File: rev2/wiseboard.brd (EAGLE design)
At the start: 87 x 67 mm, 85 parts, among them IC2 LM358MX, Q1 IRLML6402TRPBF, Q2 IRLML6402TRPBF, U1 LT1945EMSPBF, U2 BQ24210DQCT, X1 1528-1438-ND

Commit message: begin rev2 overall
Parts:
- removed C11, C12: 100nF, adafruit:C1206
- removed ESPDEBUG_1, ESPDEBUG_2: (no value), pinhead:1X08
- removed INPUTBUTTONHEADER: (no value), pinhead:1X02
- removed JP3: JUMPER, Sparkfun-Passives:SMT-JUMPER_2_NC_PASTE_NO-SILK
- removed R20, R24, R25: 10K, adafruit:R1206
- removed U$11, U$12: 1727-3473-ND, WISE:SO16
- removed U$13: FSA3157, WISE:SC70-6L
- removed X1: 1528-1438-ND, adafruit:ESP-12
- added R11, R12: 10k, resistor:R0805
- added U3: ESP-WROOM-03, esp32:ESP-WROOM-03
- C1, C16, C2, C3, C4, C5, C6, C7, C8, C9: device adafruit:C1206 -> resistor:C0805
- R1, R10, R13, R14, R2, R28, R29, R3, R30, R31, R32, R33, R34, R35, R4, R9: device adafruit:M1206 -> resistor:R0805
- R21, R22, R23, R36, R37, R38, R5, R6, R7, R8: device adafruit:R1206 -> resistor:R0805
- U$4: value HFQ339CT-ND -> FH26W-39S
- moved POWERGOOD 164.2 mm to (-74.9, 3.81), turned to 0 degrees
- moved R10 156.7 mm to (-81.3, 64.8)
- moved U2 151.2 mm to (-76.2, 82.5)
- moved R38 141.7 mm to (-74.9, 64.8), turned to 0 degrees
- moved U$14 140.6 mm to (-83.8, 77.5), turned to 0 degrees
- moved S6 140.3 mm to (-76.2, 38.1), turned to 0 degrees
- moved S5 139.5 mm to (-64.8, 38.1)
- moved D2 139.2 mm to (-82.5, 82.5), turned to 0 degrees
- moved D1 139.2 mm to (-57.1, 82.5)
- moved JP4 138.0 mm to (-50.8, 82.5), flipped to the top, turned to 0 degrees
- moved R31 136.1 mm to (-80.0, 71.1), turned to 0 degrees
- moved S4 135.5 mm to (-53.3, 38.1), turned to 0 degrees
- moved C7 134.2 mm to (-82.5, 55.9), turned to 0 degrees
- moved C9 133.4 mm to (-62.2, 64.8)
- moved CHRG/LBO 131.7 mm to (-45.7, 24.1), turned to 0 degrees
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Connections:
- removed net ADC: ESPDEBUG_1.2, R28.1, R29.2, X1.2
- removed net CH_PD: ESPDEBUG_1.3, R20.1, X1.3
- removed net GPIO12: ESPDEBUG_1.6, U$12.1, U$23.2, X1.6
- removed net GPIO13: ESPDEBUG_1.7, U$11.2, U$12.2, U$23.5, X1.7
- removed net GPIO14: ESPDEBUG_1.5, U$11.3, U$12.3, U$23.6, X1.5
- removed net GPIO15: ESPDEBUG_2.7, R25.2, U$23.1, X1.10
- removed net GPIO16: ESPDEBUG_1.4, JP3.2, X1.4
- removed net QP0: U$11.4, U$4.P$12
- removed net QP1: U$11.5, U$4.P$13
- removed net QP2: U$11.6, U$4.P$14
- removed net QP2@2: U$12.6, U$4.P$32, U$4.P$37
- removed net QP3: U$11.7, U$4.P$15
- removed net QP4: U$11.14, U$4.P$16
- removed net QP5: U$11.13, U$4.P$17
- removed net QP6: U$11.12, U$4.P$18
- removed net QP6@2: U$12.12, U$4.P$27, U$4.P$28
- removed net QP7: U$11.11, U$4.P$19
- removed net QP7@2: U$12.11, U$4.P$33, U$4.P$38
- new net 15V: U$4.P$2
- new net CKV: U$4.P$33, U$4.P$38, U3.37
- new net D0: U$4.P$12, U3.26
- new net D1: U$4.P$13, U3.27
- new net D2: U$4.P$14, U3.13
- new net D3: U$4.P$15, U3.28
- new net D4: U$4.P$16, U3.12
- new net D5: U$4.P$17, U3.29
- new net D6: U$4.P$18, U3.30
- new net D7: U$4.P$19, U3.31
- new net GMODE: U$4.P$27, U$4.P$28
- new net N$24: U3.35
- new net N$25: U3.34
- new net N$32: U3.25
- new net N$37: U3.14
- new net N$41: U3.33
- new net N$44: U3.11
- new net N$46: U3.8
- new net N$48: U3.6
- new net N$49: U3.7
- new net N$50: U3.4
- new net N$51: U3.5
- new net SPV: U$4.P$32, U$4.P$37, U3.36
- net +15V: no longer U$4.P$2
- net +3V3: now also U$4.P$10, U$4.P$29, U$4.P$30, U$4.P$35, U$4.P$36, U$4.P$4, U$4.P$8; no longer ESPDEBUG_1.8, INPUTBUTTONHEADER.1, R20.2, R24.2, U$13.5, X1.8
- net BOOSTENA: no longer ESPDEBUG_2.6, Q2.1, R24.1, X1.11
- net CL: now also U3.23; no longer ESPDEBUG_2.4, X1.13
- net GND: now also R11.1, R12.1, U3.1, U3.15, U3.38, U3.GND; no longer C11.2, C12.2, ESPDEBUG_2.8, R25.1, R29.1, U$11.8, U$12.8, U$13.2, X1.9
- net GPIO0: no longer ESPDEBUG_2.5, X1.12
- net LE: now also U3.16; no longer U$12.14
- net N$12: no longer U$13.4
- net N$26: no longer INPUTBUTTONHEADER.2, U$13.1
- net NEGEN: now also R11.2, U3.9; no longer U$12.5
- net OE: now also U3.24; no longer ESPDEBUG_2.3, X1.14
- net POSEN: now also R12.2, U3.10; no longer U$12.4
- net RESET: no longer ESPDEBUG_1.1, JP3.1, X1.1
- net RXD: no longer ESPDEBUG_2.2, U$13.6, X1.15
- net SPH: no longer U$12.13
- net TXD: no longer ESPDEBUG_2.1, X1.16
- net VBAT: no longer U$13.3
- net VDD: no longer C11.1, C12.1, U$11.1, U$11.15, U$11.16, U$12.15, U$12.16, U$4.P$10, U$4.P$29, U$4.P$30, U$4.P$35, U$4.P$36, U$4.P$4, U$4.P$8
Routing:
- net +3V3: track 287.7 -> 0.00 mm, vias 9 -> 0
- net GND: track 141.5 -> 0.00 mm, vias 38 -> 0
- net VDD: track 139.3 -> 0.00 mm, vias 8 -> 0
- net VBAT: track 125.0 -> 0.00 mm, vias 3 -> 0
- net N$26: track 115.5 -> 0.00 mm, vias 1 -> 0
- net GPIO14: track 107.6 -> 0.00 mm, vias 3 -> 0
- net GPIO12: track 101.3 -> 0.00 mm, vias 3 -> 0
- net RESET: track 98.8 -> 0.00 mm, vias 3 -> 0
- net ADC: track 80.5 -> 0.00 mm, vias 3 -> 0
- net GPIO13: track 79.2 -> 0.00 mm, vias 4 -> 0
- net GPIO0: track 72.6 -> 0.00 mm, vias 1 -> 0
- net -15V: track 71.1 -> 0.00 mm, vias 2 -> 0
- net -20V: track 67.4 -> 0.00 mm, vias 3 -> 0
- net +15V: track 66.4 -> 0.00 mm, vias 3 -> 0
- net +22V: track 61.7 -> 0.00 mm, vias 4 -> 0
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- removed copper zone on layer 1, net GND
- removed copper zone on layer 16, net GND
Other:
- board size 87 x 67 mm -> 100 x 80 mm
- board text removed: "+"
- board text removed: "0"
- board text removed: "12"
- board text removed: "13"
- board text removed: "14"
- board text removed: "15"
- board text removed: "16"
- board text removed: "3V3"
- board text removed: "ADC"
- board text removed: "BATTERY"
- board text removed: "BOOT"
- board text removed: "B_EN"
- board text removed: "Board by"
- board text removed: "CHRG"
- board text removed: "CH_PD"
- board text removed: "CL"
- board text removed: "DONE"
- board text removed: "EN TO GND"
- board text removed: "GND"
- board text removed: "GPIO0"
- board text removed: "OE"
- board text removed: "PANEL"
- board text removed: "PWRG"
- board text removed: "Project WISE"
- board text removed: "RST"
- board text removed: "RST to 16"
- board text removed: "RXD"
- board text removed: "Rev 1.6"
- board text removed: "TXD"

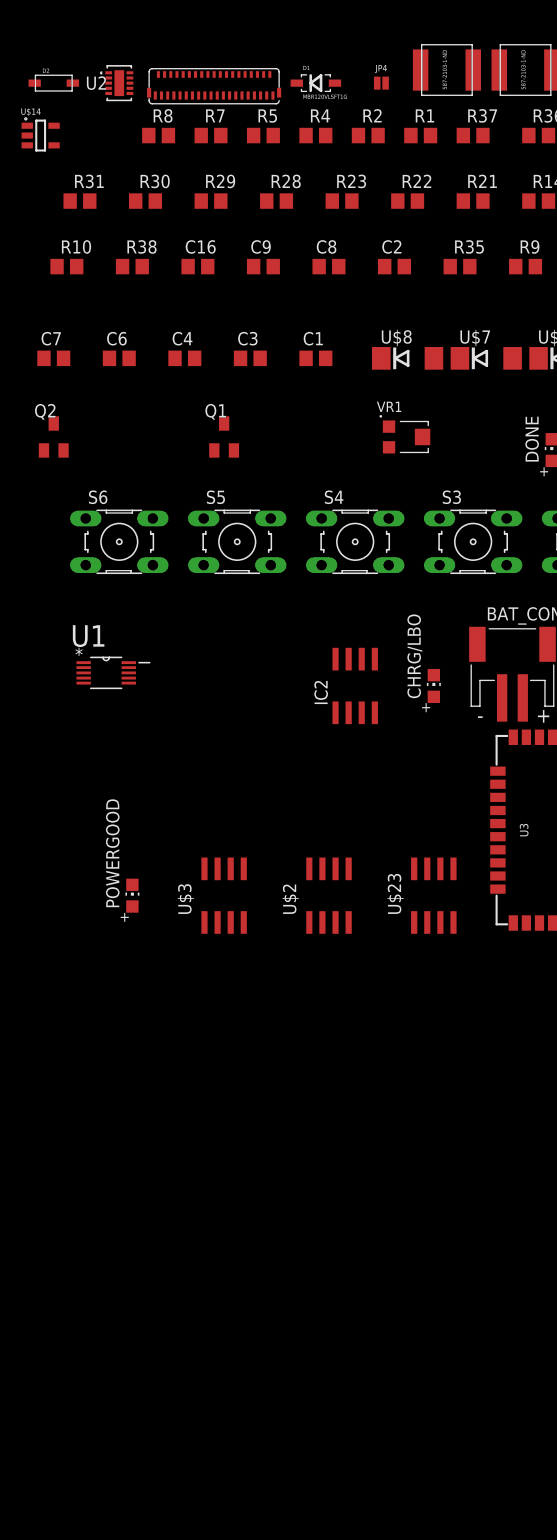
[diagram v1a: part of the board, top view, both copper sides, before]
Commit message: Connect flash chip, battery voltage, solar cell voltage
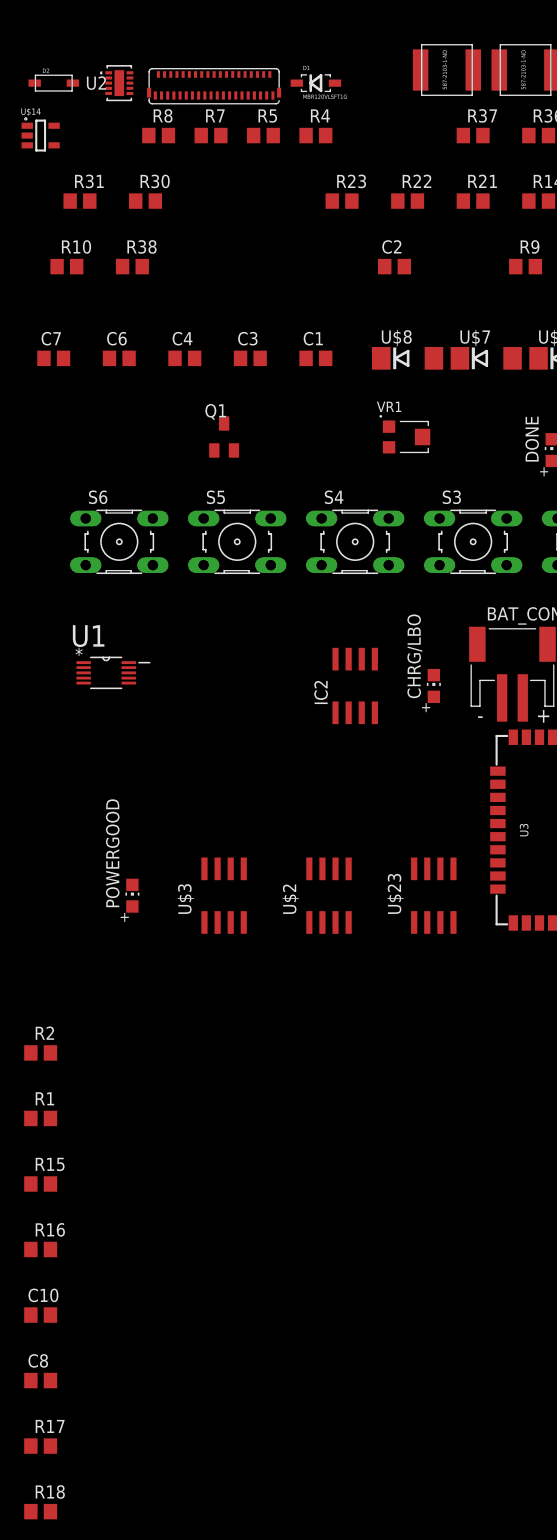
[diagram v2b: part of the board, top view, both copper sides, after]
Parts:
- removed C16, C9: 2u2F, resistor:C0805
- removed JP4: JUMPER, Sparkfun-Passives:SMT-JUMPER_2_NC_PASTE_NO-SILK
- removed Q2: IRLML6402TRPBF, IRLML6402:SOT23
- removed R28: 10k, resistor:R0805
- removed R29: 33k, resistor:R0805
- removed R35: 100k, resistor:R0805
- added C10: 10uF, resistor:C0805
- added R15, R17, R18: 10K, resistor:R0805
- added R16: 10k, resistor:R0805
- R1: value 12k -> 10K
- R2: value 47k -> 10k
- moved C8 111.5 mm to (-83.8, -43.2)
- moved R1 102.1 mm to (-83.8, -17.8)
- moved R2 94.4 mm to (-83.8, -11.4)
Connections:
- removed net 15V: U$4.P$2
- removed net BOOSTENA: R2.1
- removed net CHARGE_EN: JP4.2, U2.7
- removed net N$12: R28.2
- removed net N$13: C9.1, D1.C, U2.1
- removed net N$24: U3.35
- removed net N$25: U3.34
- removed net N$26: R35.1, S3.3, S3.4, S4.3, S4.4, S5.3, S5.4, S6.3, S6.4, S7.3, S7.4
- removed net N$3: Q1.1, R1.2, R2.2
- removed net N$32: U3.25
- removed net N$44: U3.11
- removed net N$50: U3.4
- removed net N$51: U3.5
- removed net N$7: D1.A, SOLAR.1, SOLARPIN.2
- removed net VDD: Q2.3
- new net BAT_SENS: R1.1, R15.2, U3.4
- new net CLK: U$23.6, U3.20
- new net CS: U$23.1, U3.19
- new net DPAD: R16.1, S3.3, S3.4, S4.3, S4.4, S5.3, S5.4, S6.3, S6.4, S7.3, S7.4, U3.25
- new net ESP_DI: U$23.2, U3.22
- new net ESP_DO: U$23.5, U3.21
- new net PANEL: C8.2, D1.A, D1.C, R17.2, SOLAR.1, SOLARPIN.2, U2.1
- new net PANEL_SENS: R17.1, R18.2, U3.5
- new net SUP_CTRL: Q1.1, R2.2, U3.11
- net +15V: now also U$4.P$2
- net +3V3: now also U3.2, U3.3; no longer C16.1, Q2.2
- net GND: now also C10.1, C8.1, R15.1, R16.2, R18.1, U2.7; no longer C16.2, C8.2, C9.2, JP4.1, R35.2
- net RXD: now also U3.34
- net TXD: now also U3.35
- net VBAT: now also C10.2, R1.2, R2.1; no longer C8.1, R1.1

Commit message: first run through of ERC
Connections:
- removed net N$41: U3.33
- new net N$3: C8.2, D1.C, U2.1
- net PANEL: no longer C8.2, D1.C, U2.1
- net SPH: now also U3.33
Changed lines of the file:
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@@
 </signal>
 <signal name="PANEL">
+<contactref element="R17" pad="2"/>
 <contactref element="SOLAR" pad="1"/>
 <contactref element="D1" pad="A"/>
 <contactref element="SOLARPIN" pad="2"/>
-<contactref element="D1" pad="C"/>
-<contactref element="U2" pad="1"/>
-<contactref element="C8" pad="2"/>
-<contactref element="R17" pad="2"/>
-<wire x1="-82.87" y1="-43.18" x2="-82.87" y2="-49.53" width="0" layer="19" extent="1-1"/>
-<wire x1="-25.67" y1="25.51" x2="-82.87" y2="-43.18" width="0" layer="19" extent="1-1"/>
+<wire x1="-25.67" y1="25.51" x2="-82.87" y2="-49.53" width="0" layer="19" extent="1-1"/>
 <wire x1="-19.05" y1="82.55" x2="-25.67" y2="25.51" width="0" layer="19" extent="1-1"/>
 <wire x1="-55.3" y1="82.55" x2="-19.05" y2="82.55" width="0" layer="19" extent="1-1"/>
-<wire x1="-59" y1="82.55" x2="-55.3" y2="82.55" width="0" layer="19" extent="1-1"/>
-<wire x1="-77.2287" y1="83.55" x2="-59" y2="82.55" width="0" layer="19" extent="1-1"/>
 </signal>
 <signal name="N$14">
@@
 <signal name="VBAT">
 <contactref element="D2" pad="A"/>
-<contactref element="BAT_PIN" pad="1"/>
-<contactref element="BAT_CON" pad="1"/>
 <contactref element="U2" pad="10"/>
 <contactref element="POWERGOOD" pad="A"/>
@@
 <contactref element="R1" pad="2"/>
 <contactref element="C10" pad="2"/>
+<contactref element="BAT_PIN" pad="1"/>
+<contactref element="BAT_CON" pad="1"/>
 <wire x1="-82.87" y1="-17.78" x2="-82.87" y2="-36.83" width="0" layer="19" extent="1-1"/>
 <wire x1="-84.77" y1="-11.43" x2="-82.87" y2="-17.78" width="0" layer="19" extent="1-1"/>
@@
 <signal name="SPH">
 <contactref element="U$4" pad="P$11"/>
+<contactref element="U3" pad="33"/>
+<wire x1="-69.71" y1="81.35" x2="-27.86" y2="1.16" width="0" layer="19" extent="1-1"/>
 </signal>
 <signal name="GMODE">
@@
 <signal name="N$37">
 <contactref element="U3" pad="14"/>
-</signal>
-<signal name="N$41">
-<contactref element="U3" pad="33"/>
 </signal>
 <signal name="SUP_CTRL">
@@
 <wire x1="-26.59" y1="19.16" x2="-84.77" y2="-49.53" width="0" layer="19" extent="1-1"/>
 </signal>
+<signal name="N$3">
+<contactref element="D1" pad="C"/>
+<contactref element="U2" pad="1"/>
+<contactref element="C8" pad="2"/>
+<wire x1="-77.2287" y1="83.55" x2="-82.87" y2="-43.18" width="0" layer="19" extent="1-1"/>
+<wire x1="-59" y1="82.55" x2="-77.2287" y2="83.55" width="0" layer="19" extent="1-1"/>
+</signal>
 </signals>

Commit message: Semi-Final Schematic
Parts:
- removed R16, R32: 10k, resistor:R0805
- removed R30: 1K, resistor:R0805
- removed R31: 2k, resistor:R0805
- removed R33: 12k, resistor:R0805
- removed R34: 33k, resistor:R0805
- removed S1, S2, S3, S4, S5, S6, S7: (no value), switch-omron:B3F-10XX
- added SW1, SW2: SPST_TACT-KMR2, adafruit:KMR2
- IC1: value LT1945EMSPBF -> LT1945
- IC2: value LM358MX -> LM358
- IC3: value 497-7303-1-ND -> L79L15
- IC4: value 497-7278-1-ND -> L78L15
- IC5: value W25Q32JVSSIQ -> W25Q
- moved R18 132.5 mm to (-41.9, 69.8)
- moved R17 128.8 mm to (-35.6, 69.8)
- moved C8 114.6 mm to (-41.9, 63.5)
- moved R15 112.0 mm to (-22.9, 69.8)
- moved C10 106.4 mm to (-48.3, 63.5)
- moved R1 103.4 mm to (-40.6, 76.2)
- moved U$4 102.4 mm to (3.81, 8.89), turned to 90 degrees
- moved R2 95.6 mm to (-45.7, 76.2)
- moved BAT_CON 92.9 mm to (48.3, 61.0)
- moved D3 67.7 mm to (-83.8, 81.3)
- moved C5 66.6 mm to (-83.8, 55.9)
- moved U3 64.3 mm to (21.6, 49.5), turned to 90 degrees
- moved JP1 61.2 mm to (38.1, 62.9)
- moved R13 51.4 mm to (-80.0, 63.5)
- moved R11 51.4 mm to (-67.3, 63.5)
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- renumbered U$2 to IC4, U$23 to IC5, U$3 to IC3, U1 to IC1
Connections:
- net CS renamed IC5
- removed net DPAD: R16.1, S3.3, S3.4, S4.3, S4.4, S5.3, S5.4, S6.3, S6.4, S7.3, S7.4, U3.25
- removed net N$27: R30.1, S3.1, S3.2
- removed net N$29: R31.1, S4.1, S4.2
- removed net N$31: R32.1, S5.1, S5.2
- removed net N$33: R33.1, S6.1, S6.2
- removed net N$35: R34.1, S7.1, S7.2
- new net N$7: U3.25
- net +3V3: no longer R30.2, R31.2, R32.2, R33.2, R34.2
- net -20V: now also IC3.3, IC3.6, IC3.7
- net GND: now also SW1.1, SW1.3, SW2.1, SW2.3; no longer R16.2, S1.3, S1.4, S2.3, S2.4
- net GPIO0: now also SW1.2, SW1.4; no longer S1.1, S1.2
- net RESET: now also SW2.2, SW2.4; no longer S2.1, S2.2
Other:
- board size 100 x 80 mm -> 100 x 64.8 mm
